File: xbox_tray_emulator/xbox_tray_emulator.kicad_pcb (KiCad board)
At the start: 2 copper layers, 4 parts, among them J1 to Xbox, U1 ATtiny13A-S

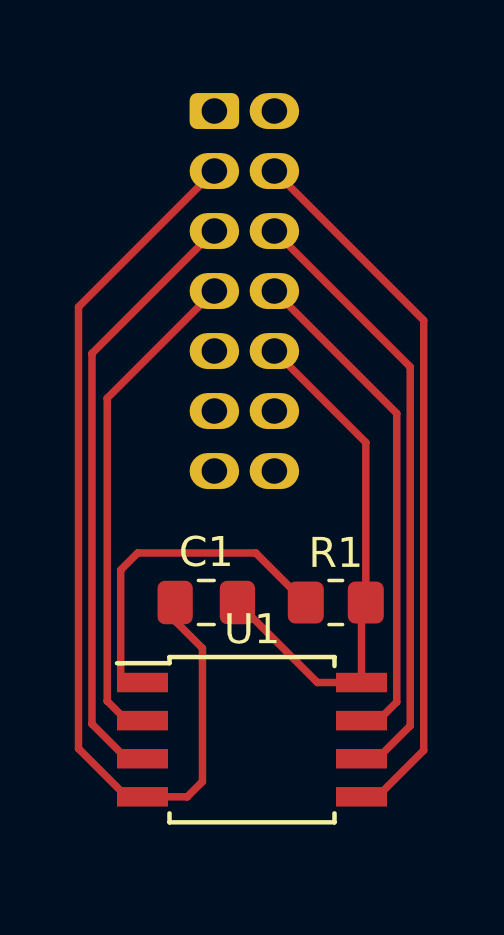
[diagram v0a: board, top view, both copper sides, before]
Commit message: set CPU frequency, correct delay
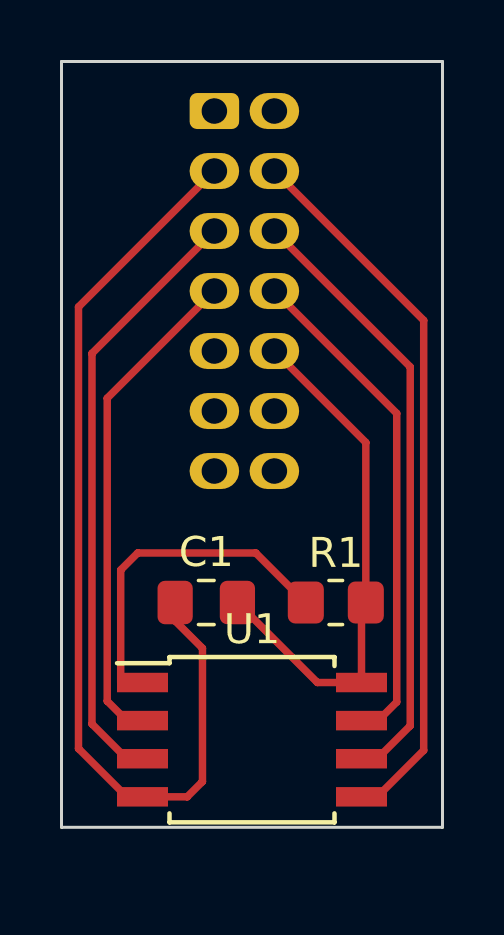
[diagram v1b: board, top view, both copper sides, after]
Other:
- board outline added: 12.7 x 25.5 mm
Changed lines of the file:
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@@
     )
   )
+  (gr_line (start 135.89 81.661) (end 148.59 81.661) (layer "Edge.Cuts") (width 0.1))
+  (gr_line (start 148.59 56.134) (end 135.89 56.134) (layer "Edge.Cuts") (width 0.1))
+  (gr_line (start 135.89 56.134) (end 135.89 81.661) (layer "Edge.Cuts") (width 0.1))
+  (gr_line (start 148.59 81.661) (end 148.59 56.134) (layer "Edge.Cuts") (width 0.1))
   (segment (start 136.45648 64.31452) (end 140.986 59.785) (width 0.25) (layer "F.Cu") (net 1))
   (segment (start 139.6785 74.168) (end 139.6785 74.7815) (width 0.25) (layer "F.Cu") (net 1))

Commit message: add PCB
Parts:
- moved J1 22.9 mm to (142.6, 80.6), turned to 90 degrees
- moved U1 19.0 mm to (142.2, 59.7), turned to 180 degrees
- moved R1 11.6 mm to (139.6, 63.9), turned to 180 degrees
- moved C1 10.7 mm to (143.8, 63.9), turned to 180 degrees
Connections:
- J1 pad 11: unconnected-(J1-Pad11) -> Net-(C1-Pad1)
- J1 pad 12: unconnected-(J1-Pad12) -> Net-(C1-Pad1)
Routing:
- net Net-(C1-Pad1): track 33.0 -> 41.3 mm, vias 0 -> 2
- net Net-(R1-Pad1): track 11.6 -> 10.5 mm
- net Net-(J1-Pad5): track 20.3 -> 20.9 mm, vias 0 -> 1
- net Net-(J1-Pad6): track 20.4 -> 20.6 mm, vias 0 -> 1
- net Net-(J1-Pad4): track 24.1 -> 24.2 mm, vias 0 -> 1
- net Net-(J1-Pad8): track 16.8 -> 16.9 mm, vias 0 -> 1
- net Net-(J1-Pad7): vias 0 -> 2
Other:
- board size 12.7 x 25.5 mm -> 10.2 x 26.4 mm

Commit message: PCB cleanup
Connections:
- J1 pad 2: unconnected-(J1-Pad2) -> Net-(C1-Pad2)
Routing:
- net Net-(C1-Pad2): track 17.7 -> 27.1 mm
- net Net-(C1-Pad1): track 41.3 -> 32.7 mm
- net Net-(J1-Pad5): track 20.9 -> 19.9 mm
- net Net-(J1-Pad7): track 17.4 -> 16.9 mm, vias 2 -> 1
